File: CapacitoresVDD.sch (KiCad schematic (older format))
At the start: 7 parts

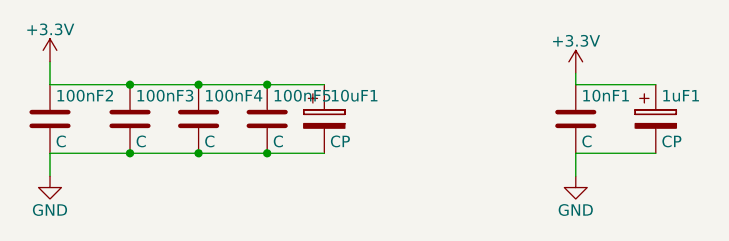
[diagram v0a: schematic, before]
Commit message: ajustes
corrigido a inversão do valor com referencia
diminuido a largura da trilha.
trocado componentes por smd
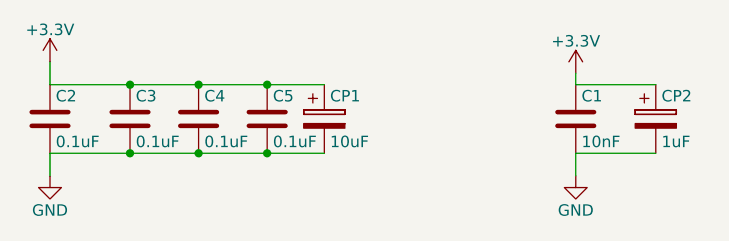
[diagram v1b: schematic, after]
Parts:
- C1: renamed from 10nF1; value C -> 10nF
- C2: renamed from 100nF2; value C -> 0.1uF
- C3: renamed from 100nF3; value C -> 0.1uF
- C4: renamed from 100nF4; value C -> 0.1uF
- C5: renamed from 100nF5; value C -> 0.1uF
- CP1: renamed from 10uF1; value CP -> 10uF
- CP2: renamed from 1uF1; value CP -> 1uF
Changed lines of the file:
@@
 $EndDescr
 $Comp
-L C 100nF2
+L C C2
 U 1 1 5717E12D
 P 4750 3900
-F 0 "100nF2" H 4775 4000 50  0000 L CNN
-F 1 "C" H 4775 3800 50  0000 L CNN
+F 0 "C2" H 4775 4000 50  0000 L CNN
+F 1 "0.1uF" H 4775 3800 50  0000 L CNN
 F 2 "Capacitors_SMD:C_0603_HandSoldering" H 4788 3750 50  0001 C CNN
 F 3 "" H 4750 3900 50  0000 C CNN
@@
 $EndComp
 $Comp
-L C 100nF3
+L C C3
 U 1 1 5717E146
 P 5100 3900
-F 0 "100nF3" H 5125 4000 50  0000 L CNN
-F 1 "C" H 5125 3800 50  0000 L CNN
+F 0 "C3" H 5125 4000 50  0000 L CNN
+F 1 "0.1uF" H 5125 3800 50  0000 L CNN
 F 2 "Capacitors_SMD:C_0603_HandSoldering" H 5138 3750 50  0001 C CNN
 F 3 "" H 5100 3900 50  0000 C CNN
@@
 $EndComp
 $Comp
-L C 100nF4
+L C C4
 U 1 1 5717E209
 P 5400 3900
-F 0 "100nF4" H 5425 4000 50  0000 L CNN
-F 1 "C" H 5425 3800 50  0000 L CNN
+F 0 "C4" H 5425 4000 50  0000 L CNN
+F 1 "0.1uF" H 5425 3800 50  0000 L CNN
 F 2 "Capacitors_SMD:C_0603_HandSoldering" H 5438 3750 50  0001 C CNN
 F 3 "" H 5400 3900 50  0000 C CNN
@@
 $EndComp
 $Comp
-L C 100nF5
+L C C5
 U 1 1 5717E232
 P 5700 3900
-F 0 "100nF5" H 5725 4000 50  0000 L CNN
-F 1 "C" H 5725 3800 50  0000 L CNN
+F 0 "C5" H 5725 4000 50  0000 L CNN
+F 1 "0.1uF" H 5725 3800 50  0000 L CNN
 F 2 "Capacitors_SMD:C_0603_HandSoldering" H 5738 3750 50  0001 C CNN
 F 3 "" H 5700 3900 50  0000 C CNN
@@
 $EndComp
 $Comp
-L C 10nF1
+L C C1
 U 1 1 5717E4D7
 P 7050 3900
-F 0 "10nF1" H 7075 4000 50  0000 L CNN
-F 1 "C" H 7075 3800 50  0000 L CNN
+F 0 "C1" H 7075 4000 50  0000 L CNN
+F 1 "10nF" H 7075 3800 50  0000 L CNN
 F 2 "Capacitors_SMD:C_0603_HandSoldering" H 7088 3750 50  0001 C CNN
 F 3 "" H 7050 3900 50  0000 C CNN
@@
 $EndComp
 $Comp
-L CP 10uF1
+L CP CP1
 U 1 1 5717E506
 P 5950 3900
-F 0 "10uF1" H 5975 4000 50  0000 L CNN
-F 1 "CP" H 5975 3800 50  0000 L CNN
+F 0 "CP1" H 5975 4000 50  0000 L CNN
+F 1 "10uF" H 5975 3800 50  0000 L CNN
 F 2 "Capacitors_SMD:C_0603_HandSoldering" H 5988 3750 50  0001 C CNN
 F 3 "" H 5950 3900 50  0000 C CNN
@@
 Connection ~ 5700 4050
 $Comp
-L +3.3V #PWR013
+L +3.3V #PWR13
 U 1 1 5717E646
 P 4750 3650
-F 0 "#PWR013" H 4750 3500 50  0001 C CNN
+F 0 "#PWR13" H 4750 3500 50  0001 C CNN
 F 1 "+3.3V" H 4750 3790 50  0000 C CNN
 F 2 "" H 4750 3650 50  0000 C CNN
@@
 	4750 3750 4750 3650
 $Comp
-L GND #PWR014
+L GND #PWR14
 U 1 1 5717E67E
 P 4750 4150
-F 0 "#PWR014" H 4750 3900 50  0001 C CNN
+F 0 "#PWR14" H 4750 3900 50  0001 C CNN
 F 1 "GND" H 4750 4000 50  0000 C CNN
 F 2 "" H 4750 4150 50  0000 C CNN
@@
 	4750 4150 4750 4050
 $Comp
-L CP 1uF1
+L CP CP2
 U 1 1 5717E76D
 P 7400 3900
-F 0 "1uF1" H 7425 4000 50  0000 L CNN
-F 1 "CP" H 7425 3800 50  0000 L CNN
+F 0 "CP2" H 7425 4000 50  0000 L CNN
+F 1 "1uF" H 7425 3800 50  0000 L CNN
 F 2 "Capacitors_SMD:C_0603_HandSoldering" H 7438 3750 50  0001 C CNN
 F 3 "" H 7400 3900 50  0000 C CNN
@@
 	7050 4050 7400 4050
 $Comp
-L +3.3V #PWR015
+L +3.3V #PWR15
 U 1 1 5717E9D6
 P 7050 3700
-F 0 "#PWR015" H 7050 3550 50  0001 C CNN
+F 0 "#PWR15" H 7050 3550 50  0001 C CNN
 F 1 "+3.3V" H 7050 3840 50  0000 C CNN
 F 2 "" H 7050 3700 50  0000 C CNN
@@
 	7050 3750 7050 3700
 $Comp
-L GND #PWR016
+L GND #PWR16
 U 1 1 5717EA1D
 P 7050 4150
-F 0 "#PWR016" H 7050 3900 50  0001 C CNN
+F 0 "#PWR16" H 7050 3900 50  0001 C CNN
 F 1 "GND" H 7050 4000 50  0000 C CNN
 F 2 "" H 7050 4150 50  0000 C CNN
